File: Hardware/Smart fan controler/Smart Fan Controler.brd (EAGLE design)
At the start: 71.9 x 106.2 mm, 26 parts

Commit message: Main board Done
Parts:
- added J3: (no value), SparkFun-Connectors:1X05_NO_SILK
- added R4, R5: (no value), rcl:R0805
- added U$4: AIR_QUALITY_SENSOR, Smart fan:AIR_SENSOR
- moved C2 43.3 mm to (-19.3, 81.5), turned to 180 degrees
- moved C1 37.1 mm to (-14.6, 80.0), turned to 90 degrees
- moved U$1 36.7 mm to (-19.0, 78.0), turned to 270 degrees
- moved J5 18.0 mm to (-30.6, 82.2)
- moved J6 6.84 mm to (26.5, 39.9)
- moved U$2 5.00 mm to (3.19, 71.0)
- moved J1 4.47 mm to (27.2, 97.0)
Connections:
- removed net N$12: J6.6
- removed net N$13: J6.5
- removed net N$14: U$1.P$8
- removed net N$15: U$1.P$7
- removed net N$16: U$1.P$6
- removed net N$17: J6.4
- removed net N$18: J6.3
- removed net N$6: J5.6
- removed net N$7: J5.5
- removed net N$8: J5.4
- removed net N$9: J5.3
- new net 12VIN: J1.1, R4.2
- new net VOUT: J3.2, U$2.D8
- new net VOUT2: J3.5, U$2.D9
- new net VTH: J3.4, U$2.A5
- net 0: now also J3.3, R5.1
- net 12V: now also R4.1, R5.2; no longer J1.1
- net 5V: now also J3.1, J5.6, J6.6
- net CS1: now also U$2.A4
- net CS2: now also U$2.A6
- net CS3: now also U$2.A7
- net MISO: now also J5.3, J6.3, U$1.P$6
- net MOSI: now also J5.4, J6.4, U$1.P$7
- net PWM2: no longer U$2.D6
- net PWM3: now also U$2.D6
- net SCLK: now also J5.5, J6.5, U$1.P$8
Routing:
- net 5V: track 0.00 -> 120.3 mm
- net SCLK: track 0.00 -> 103.3 mm, vias 0 -> 3
- net MISO: track 0.00 -> 90.6 mm
- net MOSI: track 0.00 -> 84.5 mm, vias 0 -> 2
- net SENSE1: track 0.00 -> 66.6 mm, vias 0 -> 2
- net CS3: track 0.00 -> 59.4 mm, vias 0 -> 3
- net PWM1: track 0.00 -> 52.4 mm, vias 0 -> 2
- net VOUT: track 0.00 -> 46.3 mm, vias 0 -> 1
- net SENSE3: track 18.9 -> 64.7 mm, vias 2 -> 4
- net PWM3: track 18.2 -> 61.5 mm, vias 2 -> 4
- net CS2: track 0.00 -> 40.5 mm, vias 0 -> 1
- net VOUT2: track 0.00 -> 39.0 mm
- net CS1: track 0.00 -> 38.5 mm, vias 0 -> 3
- net VTH: track 0.00 -> 36.4 mm, vias 0 -> 2
- net PWM2: track 19.1 -> 46.4 mm, vias 2 -> 4
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
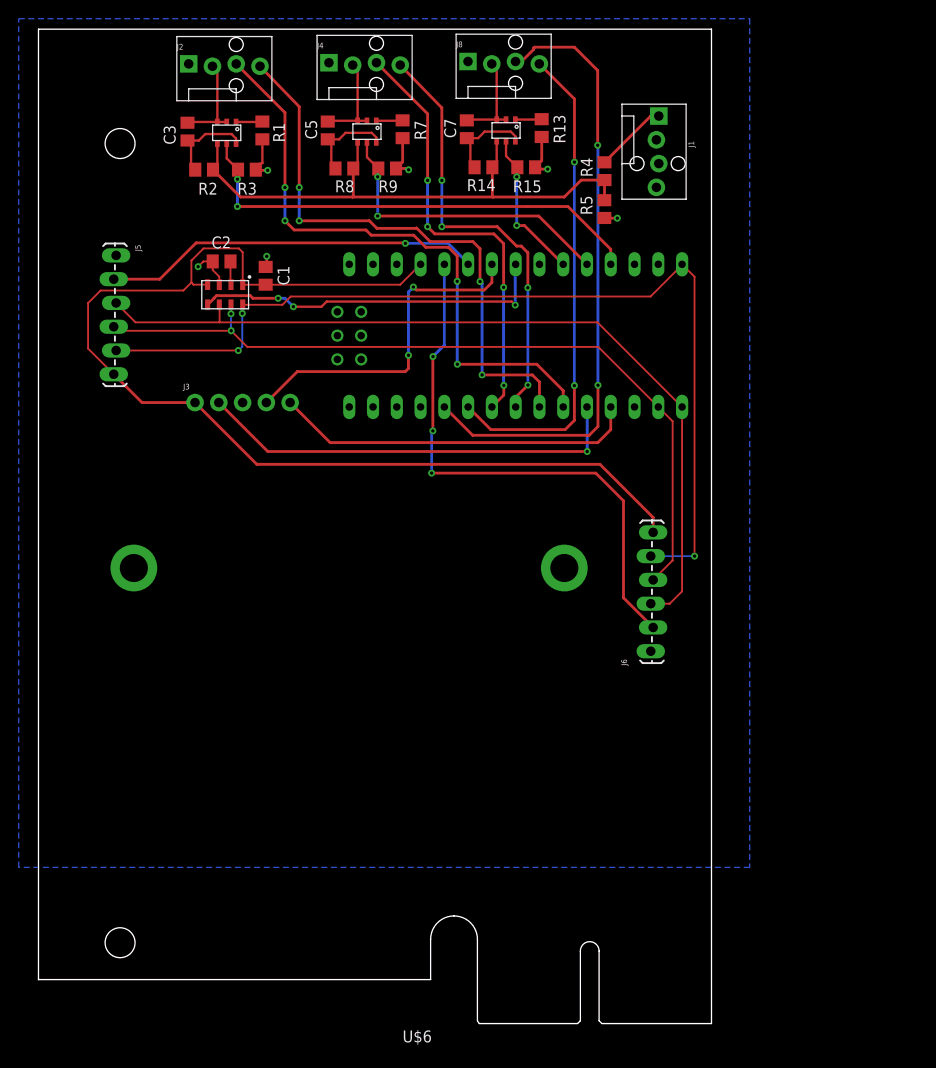
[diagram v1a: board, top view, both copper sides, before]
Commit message: added breakout board
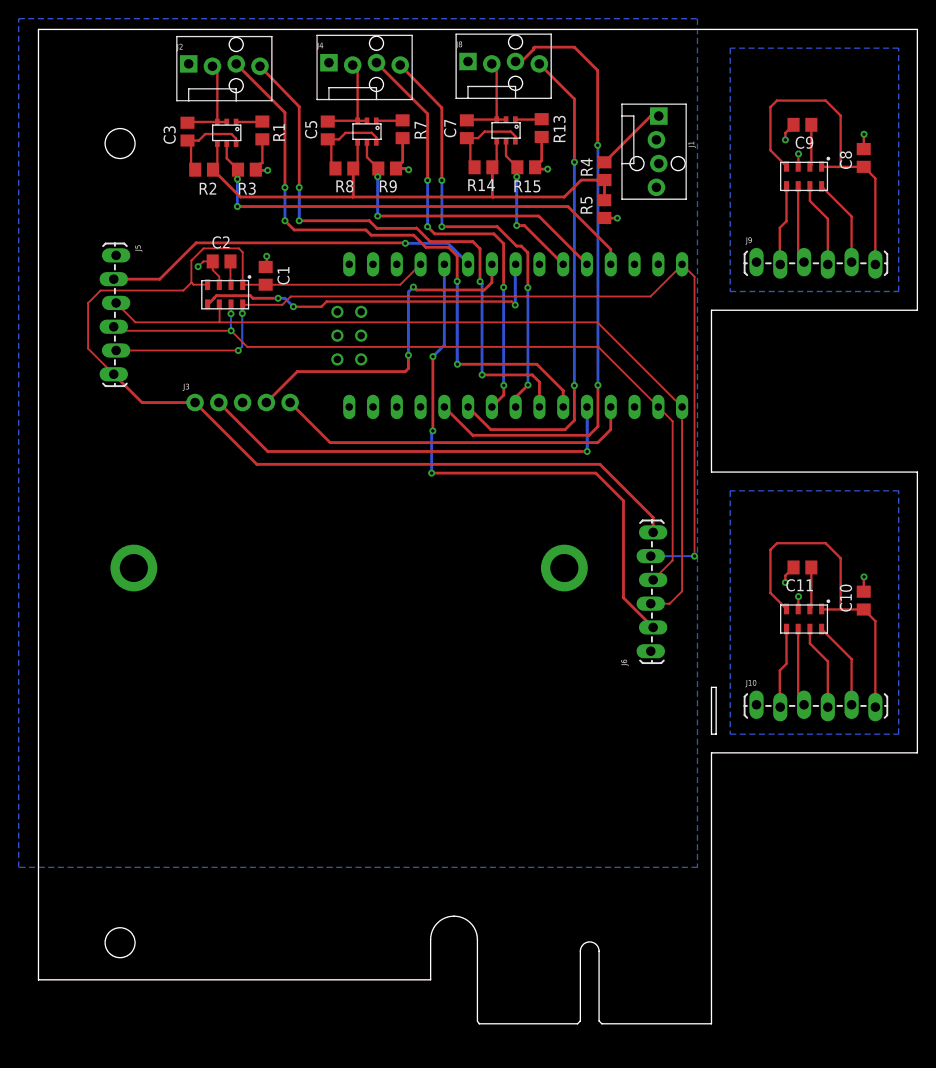
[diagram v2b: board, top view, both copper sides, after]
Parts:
- removed U$6: PCI-E-X1-BOARD, Smart fan:PCIE_X1_FORM
- added C10, C11, C8, C9: (no value), rcl:C0805
- added J10, J9: (no value), SparkFun-Connectors:1X06_LOCK_LONGPADS
- added U$7, U$9: MPL115A1, Smart fan:MPL115A1
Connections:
- new net CS_REMOTE: J10.2, J9.2, U$7.P$5, U$9.P$5
- new net N$4: C9.1, U$7.P$2
- new net N$5: C11.1, U$9.P$2
- net 0: now also C10.2, C11.2, C8.2, C9.2, J10.1, J9.1, U$7.P$3, U$9.P$3
- net 5V: now also C10.1, C8.1, J10.6, J9.6, U$7.P$1, U$7.P$4, U$9.P$1, U$9.P$4
- net MISO: now also J10.3, J9.3, U$7.P$6, U$9.P$6
- net MOSI: now also J10.4, J9.4, U$7.P$7, U$9.P$7
- net SCLK: now also J10.5, J9.5, U$7.P$8, U$9.P$8
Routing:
- net 5V: track 120.3 -> 193.3 mm
- net SCLK: track 103.3 -> 122.1 mm
- net MOSI: track 84.5 -> 102.8 mm
- net CS_REMOTE: track 0.00 -> 17.3 mm
- net MISO: track 90.6 -> 107.3 mm
- net 0: track 21.9 -> 31.7 mm, vias 6 -> 12
- net N$5: track 0.00 -> 4.50 mm
- net N$4: track 0.00 -> 4.50 mm
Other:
- board size 71.9 x 106.2 mm -> 93.9 x 106.2 mm
- board text added: ">NAME"
- board text added: ">VALUE"
